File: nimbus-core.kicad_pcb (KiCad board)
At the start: 4 copper layers, 61.9 x 61.9 mm, 71 parts, among them J1 QTE-020-03-L-D-A, J2 QSE-020-01-L-D-A, J3 532614006, J4 USB4105-GF-A-120, J5 532614006, J6 532614006, U1 STM32F405VGT7, U10 Yellow, U4 SN65HVD233-Q1, U8 SN65HVD1782-Q1, U9 USBLC6-2P6, Y1 25MHz

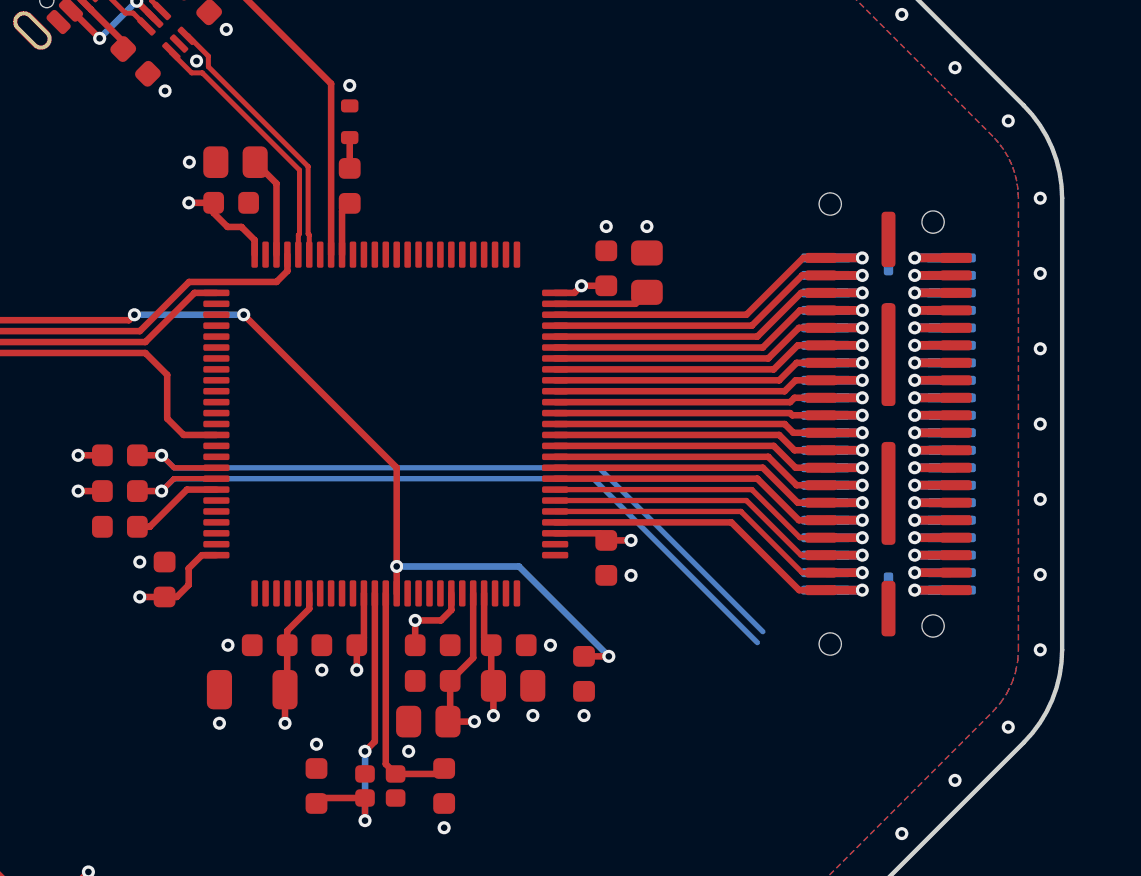
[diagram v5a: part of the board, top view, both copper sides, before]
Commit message: Moved passthrough connector to allow for connections on far the far side
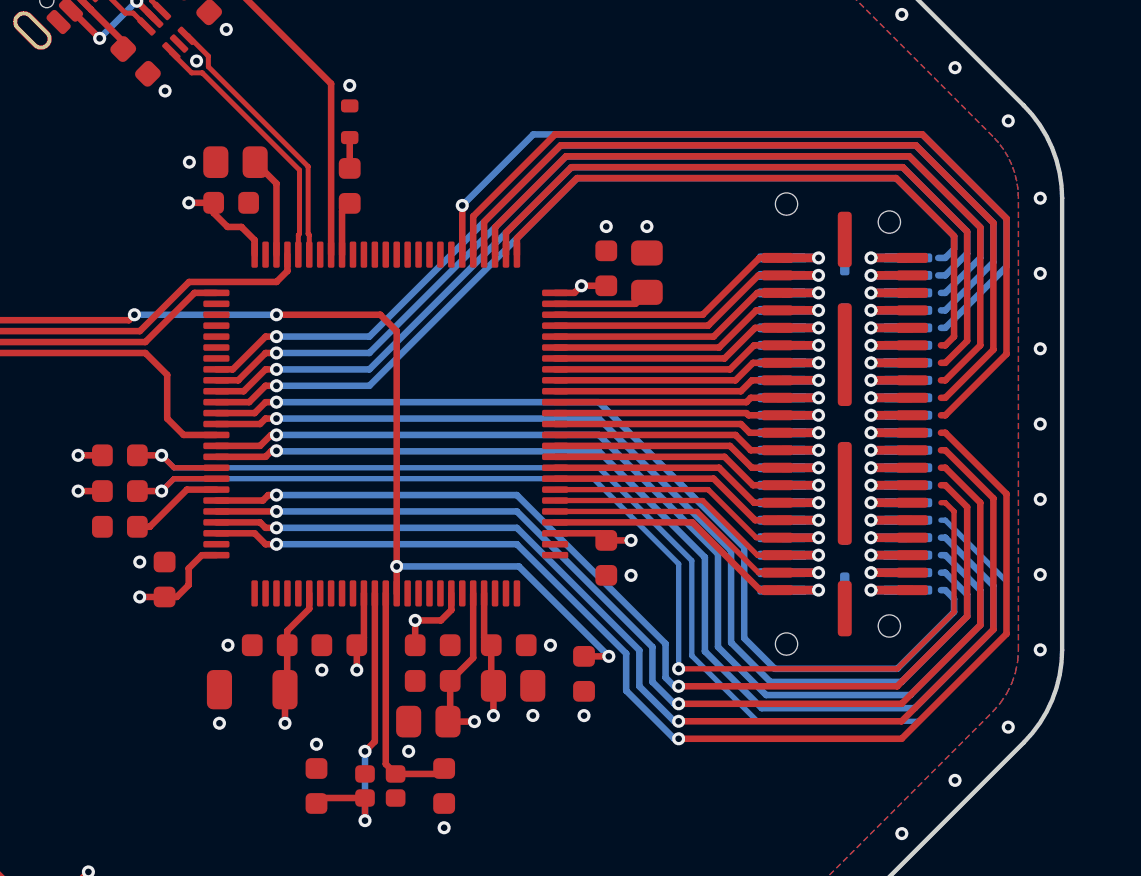
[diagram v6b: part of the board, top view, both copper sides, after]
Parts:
- moved J1 2.00 mm to (169.5, 105.0)
- moved J2 2.00 mm to (169.5, 105.0)
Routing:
- net unconnected-(U1F-PE1-Pad98): track 0.00 -> 53.6 mm, vias 0 -> 2
- net unconnected-(U1F-PE0-Pad97): track 0.00 -> 51.3 mm, vias 0 -> 2
- net unconnected-(U1C-PB5-Pad91): track 0.00 -> 49.9 mm, vias 0 -> 1
- net unconnected-(U1C-PB9-Pad96): track 0.00 -> 49.1 mm, vias 0 -> 2
- net unconnected-(U1C-PB4-Pad90): track 0.00 -> 48.0 mm, vias 0 -> 1
- net /PWR_ALERT: track 0.00 -> 46.9 mm, vias 0 -> 2
- net unconnected-(U1E-PD2-Pad83): track 0.00 -> 46.4 mm, vias 0 -> 1
- net unconnected-(U1E-PD7-Pad88): track 0.00 -> 45.8 mm, vias 0 -> 1
- net unconnected-(U1E-PD3-Pad84): track 0.00 -> 44.4 mm, vias 0 -> 1
- net /FIRE_PYRO1: track 0.00 -> 43.9 mm, vias 0 -> 1
- net unconnected-(U1E-PD4-Pad85): track 0.00 -> 42.6 mm, vias 0 -> 1
- net /FIRE_PYRO2: track 0.00 -> 40.6 mm, vias 0 -> 1
- net unconnected-(U1E-PD8-Pad55): track 0.00 -> 39.7 mm
- net unconnected-(U1C-PB15-Pad54): track 0.00 -> 36.8 mm
- net unconnected-(U1E-PD9-Pad56): track 0.00 -> 36.5 mm, vias 0 -> 1
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
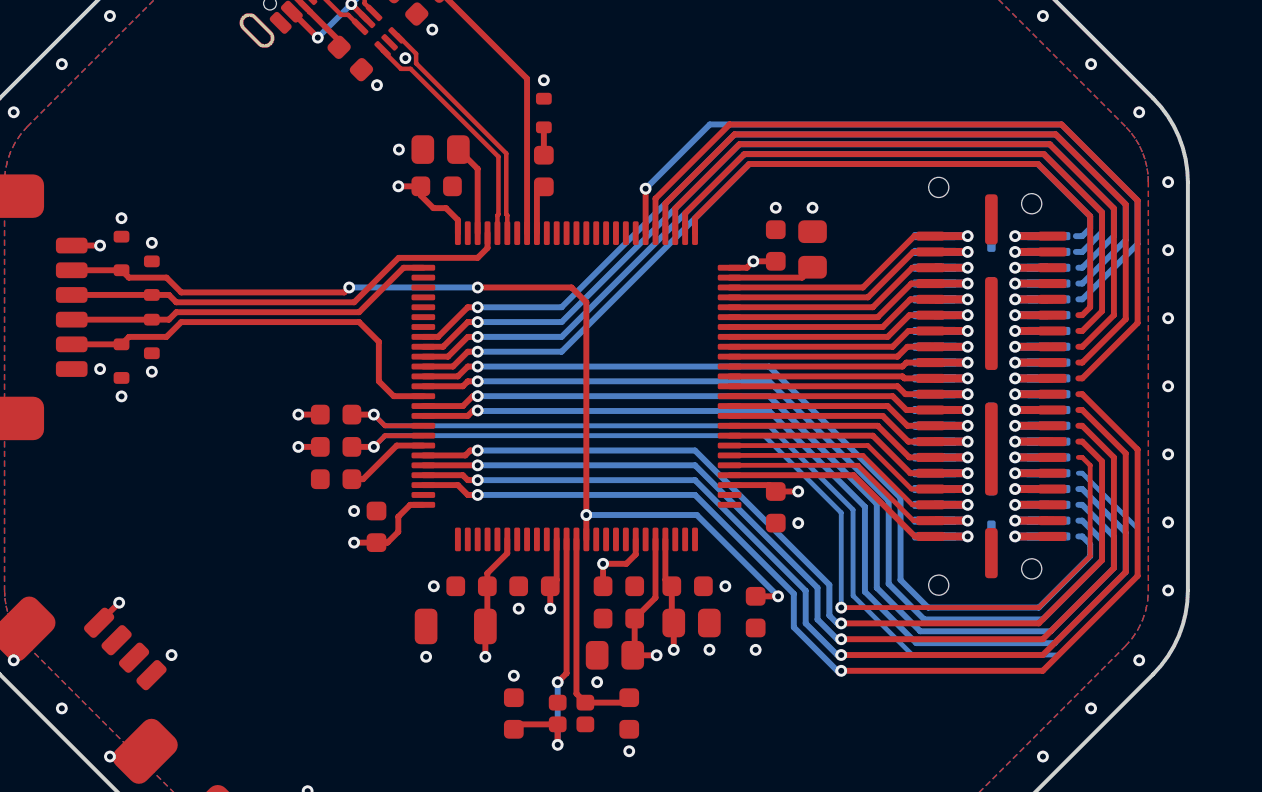
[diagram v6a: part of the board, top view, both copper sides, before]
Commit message: Rename all passthrough pins to their corresponding MCU pin name, fix typo on SPI pins
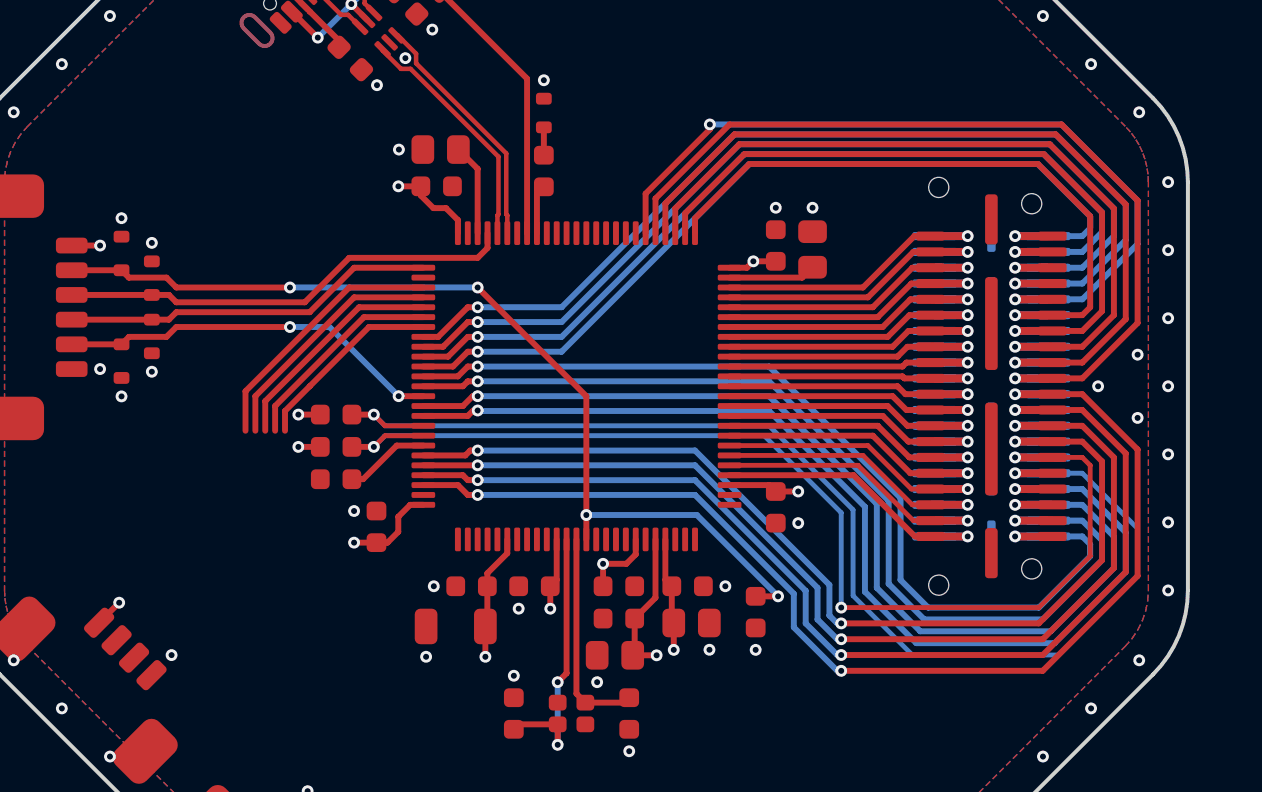
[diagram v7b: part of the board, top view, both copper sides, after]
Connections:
- net /ACCEL_IRQ renamed /PE9
- net /GNSS_RESET renamed /PA1
- net /GNSS_SAFEBOOT renamed /PA0
- net /GNSS_TIMEPULSE renamed /PA2
- net /IMU_IRQ renamed /PE7
- net /PASSTHROUGH_P16 renamed /PE10
- net /PASSTHROUGH_P2 renamed /PB11
- net /PASSTHROUGH_P24 renamed /PB2
- net /PASSTHROUGH_P26 renamed /PB1
- net /PASSTHROUGH_P28 renamed /PB0
- net /PASSTHROUGH_P30 renamed /PC5
- net /PASSTHROUGH_P34 renamed /SPI1_MOSI
- net /PASSTHROUGH_P36 renamed /SPI1_MISO
- net /PASSTHROUGH_P38 renamed /SPI1_SCK
- net /PASSTHROUGH_P4 renamed /PB10
- J1 pad 1: /PASSTHROUGH_P1 -> /PD5
- J1 pad 10: /PASSTHROUGH_P10 -> /PE13
- J1 pad 11: /PASSTHROUGH_P11 -> /PB12
- J1 pad 12: /PASSTHROUGH_P12 -> /PE12
- J1 pad 13: /PASSTHROUGH_P13 -> /PB13
- J1 pad 14: /PASSTHROUGH_P14 -> /PE11
- J1 pad 15: /PASSTHROUGH_P15 -> /PB14
- J1 pad 17: /PASSTHROUGH_P17 -> /PB15
- J1 pad 19: /PASSTHROUGH_P19 -> /PD8
- J1 pad 20: /PASSTHROUGH_P20 -> /PE8
- J1 pad 21: /PASSTHROUGH_P21 -> /PE1
- J1 pad 23: /PASSTHROUGH_P23 -> /PE0
- J1 pad 25: /PASSTHROUGH_P25 -> /PB9
- J1 pad 27: /PASSTHROUGH_P27 -> /PB8
- J1 pad 29: /PASSTHROUGH_P29 -> /I2C1_SDA
- J1 pad 3: /PASSTHROUGH_P3 -> /PD4
- J1 pad 31: /PASSTHROUGH_P31 -> /I2C1_SCL
- J1 pad 32: /PASSTHROUGH_P32 -> /PC4
- J1 pad 33: /PASSTHROUGH_P33 -> /PB5
- J1 pad 35: /PASSTHROUGH_P35 -> /PB4
- J1 pad 37: /PASSTHROUGH_P37 -> /PD7
- J1 pad 39: /PASSTHROUGH_P39 -> /PD6
- J1 pad 40: /PASSTHROUGH_P40 -> /PA4
- J1 pad 5: /PASSTHROUGH_P5 -> /PD3
- J1 pad 6: /PASSTHROUGH_P6 -> /PE15
- J1 pad 7: /PASSTHROUGH_P7 -> /PD2
- J1 pad 8: /PASSTHROUGH_P8 -> /PE14
- J1 pad 9: /PASSTHROUGH_P9 -> /PD9
- J2 pad 1: /PASSTHROUGH_P1 -> /PD5
- J2 pad 10: /PASSTHROUGH_P10 -> /PE13
- J2 pad 11: /PASSTHROUGH_P11 -> /PB12
- J2 pad 12: /PASSTHROUGH_P12 -> /PE12
- J2 pad 13: /PASSTHROUGH_P13 -> /PB13
- J2 pad 14: /PASSTHROUGH_P14 -> /PE11
- J2 pad 15: /PASSTHROUGH_P15 -> /PB14
- J2 pad 17: /PASSTHROUGH_P17 -> /PB15
- J2 pad 19: /PASSTHROUGH_P19 -> /PD8
- J2 pad 20: /PASSTHROUGH_P20 -> /PE8
- J2 pad 21: /PASSTHROUGH_P21 -> /PE1
- J2 pad 23: /PASSTHROUGH_P23 -> /PE0
- J2 pad 25: /PASSTHROUGH_P25 -> /PB9
- J2 pad 27: /PASSTHROUGH_P27 -> /PB8
- J2 pad 29: /PASSTHROUGH_P29 -> /I2C1_SDA
- J2 pad 3: /PASSTHROUGH_P3 -> /PD4
- J2 pad 31: /PASSTHROUGH_P31 -> /I2C1_SCL
- J2 pad 32: /PASSTHROUGH_P32 -> /PC4
- J2 pad 33: /PASSTHROUGH_P33 -> /PB5
- J2 pad 35: /PASSTHROUGH_P35 -> /PB4
- J2 pad 37: /PASSTHROUGH_P37 -> /PD7
- J2 pad 39: /PASSTHROUGH_P39 -> /PD6
- J2 pad 40: /PASSTHROUGH_P40 -> /PC4
- J2 pad 5: /PASSTHROUGH_P5 -> /PD3
- J2 pad 6: /PASSTHROUGH_P6 -> /PE15
- J2 pad 7: /PASSTHROUGH_P7 -> /PD2
- J2 pad 8: /PASSTHROUGH_P8 -> /PE14
- J2 pad 9: /PASSTHROUGH_P9 -> /PD9
- U1 pad 1: unconnected-(U1F-PE2-Pad1) -> /PE2
- U1 pad 15: unconnected-(U1D-PC0-Pad15) -> /PC0
- U1 pad 16: unconnected-(U1D-PC1-Pad16) -> /PC1
- U1 pad 17: unconnected-(U1D-PC2-Pad17) -> /PC2
- U1 pad 18: unconnected-(U1D-PC3-Pad18) -> /PC3
- U1 pad 2: unconnected-(U1F-PE3-Pad2) -> /PE3
- U1 pad 26: /~{GNSS_SS} -> /PA3
- U1 pad 29: /PASSTHROUGH_P40 -> /PA4
- U1 pad 3: unconnected-(U1F-PE4-Pad3) -> /PE4
- U1 pad 33: /PASSTHROUGH_P32 -> /PC4
- U1 pad 39: /PASSTHROUGH_P20 -> /PE8
- U1 pad 4: unconnected-(U1F-PE5-Pad4) -> /PE5
- U1 pad 42: /PASSTHROUGH_P14 -> /PE11
- U1 pad 43: /PASSTHROUGH_P12 -> /PE12
- U1 pad 44: /PASSTHROUGH_P10 -> /PE13
- U1 pad 45: /PASSTHROUGH_P8 -> /PE14
- U1 pad 46: /PASSTHROUGH_P6 -> /PE15
- U1 pad 5: unconnected-(U1F-PE6-Pad5) -> /PE6
- U1 pad 51: /RADIO_RESET -> /PB12
- U1 pad 52: /RADIO_ANT_EN -> /PB13
- U1 pad 53: unconnected-(U1C-PB14-Pad53) -> /PB14
- U1 pad 54: unconnected-(U1C-PB15-Pad54) -> /PB15
- U1 pad 55: unconnected-(U1E-PD8-Pad55) -> /PD8
- U1 pad 56: unconnected-(U1E-PD9-Pad56) -> /PD9
- U1 pad 57: unconnected-(U1E-PD10-Pad57) -> /PD10
- U1 pad 58: unconnected-(U1E-PD11-Pad58) -> /PD11
- U1 pad 59: unconnected-(U1E-PD12-Pad59) -> /PD12
- U1 pad 60: unconnected-(U1E-PD13-Pad60) -> /PD13
- U1 pad 61: unconnected-(U1E-PD14-Pad61) -> /PD14
- U1 pad 62: unconnected-(U1E-PD15-Pad62) -> /PD15
- U1 pad 63: unconnected-(U1D-PC6-Pad63) -> /PC6
- U1 pad 64: unconnected-(U1D-PC7-Pad64) -> /PC7
- U1 pad 65: unconnected-(U1D-PC8-Pad65) -> /PC8
- U1 pad 66: unconnected-(U1D-PC9-Pad66) -> /PC9
- U1 pad 69: unconnected-(U1B-PA10-Pad69) -> /PA10
- U1 pad 7: unconnected-(U1D-PC13-Pad7) -> /PC13
- U1 pad 8: unconnected-(U1D-PC14-Pad8) -> /PC14
- U1 pad 83: unconnected-(U1E-PD2-Pad83) -> /PD2
- U1 pad 84: unconnected-(U1E-PD3-Pad84) -> /PD3
- U1 pad 85: unconnected-(U1E-PD4-Pad85) -> /PD4
- U1 pad 86: /FIRE_PYRO2 -> /PD5
- U1 pad 87: /FIRE_PYRO1 -> /PD6
- U1 pad 88: unconnected-(U1E-PD7-Pad88) -> /PD7
- U1 pad 9: unconnected-(U1D-PC15-Pad9) -> /PC15
- U1 pad 90: unconnected-(U1C-PB4-Pad90) -> /PB4
- U1 pad 91: unconnected-(U1C-PB5-Pad91) -> /PB5
- U1 pad 95: /PWR_ALERT -> /PB8
- U1 pad 96: unconnected-(U1C-PB9-Pad96) -> /PB9
- U1 pad 97: unconnected-(U1F-PE0-Pad97) -> /PE0
- U1 pad 98: unconnected-(U1F-PE1-Pad98) -> /PE1
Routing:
- net /PE1: track 0.00 -> 58.5 mm, vias 0 -> 3
- net /PE0: track 0.00 -> 56.2 mm, vias 0 -> 3
- net /PB5: track 0.00 -> 54.9 mm, vias 0 -> 2
- net /PB9: track 0.00 -> 54.0 mm, vias 0 -> 3
- net unconnected-(U1F-PE1-Pad98): track 53.6 -> 0.00 mm, vias 2 -> 0
- net /PB4: track 0.00 -> 53.0 mm, vias 0 -> 2
- net /PB8: track 0.00 -> 51.8 mm, vias 0 -> 3
- net /PD2: track 0.00 -> 51.5 mm, vias 0 -> 2
- net unconnected-(U1F-PE0-Pad97): track 51.3 -> 0.00 mm, vias 2 -> 0
- net /PD7: track 0.00 -> 50.8 mm, vias 0 -> 2
- net unconnected-(U1C-PB5-Pad91): track 49.9 -> 0.00 mm, vias 1 -> 0
- net /PD3: track 0.00 -> 49.5 mm, vias 0 -> 2
- net unconnected-(U1C-PB9-Pad96): track 49.1 -> 0.00 mm, vias 2 -> 0
- net /PD6: track 0.00 -> 49.0 mm, vias 0 -> 2
- net unconnected-(U1C-PB4-Pad90): track 48.0 -> 0.00 mm, vias 1 -> 0
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
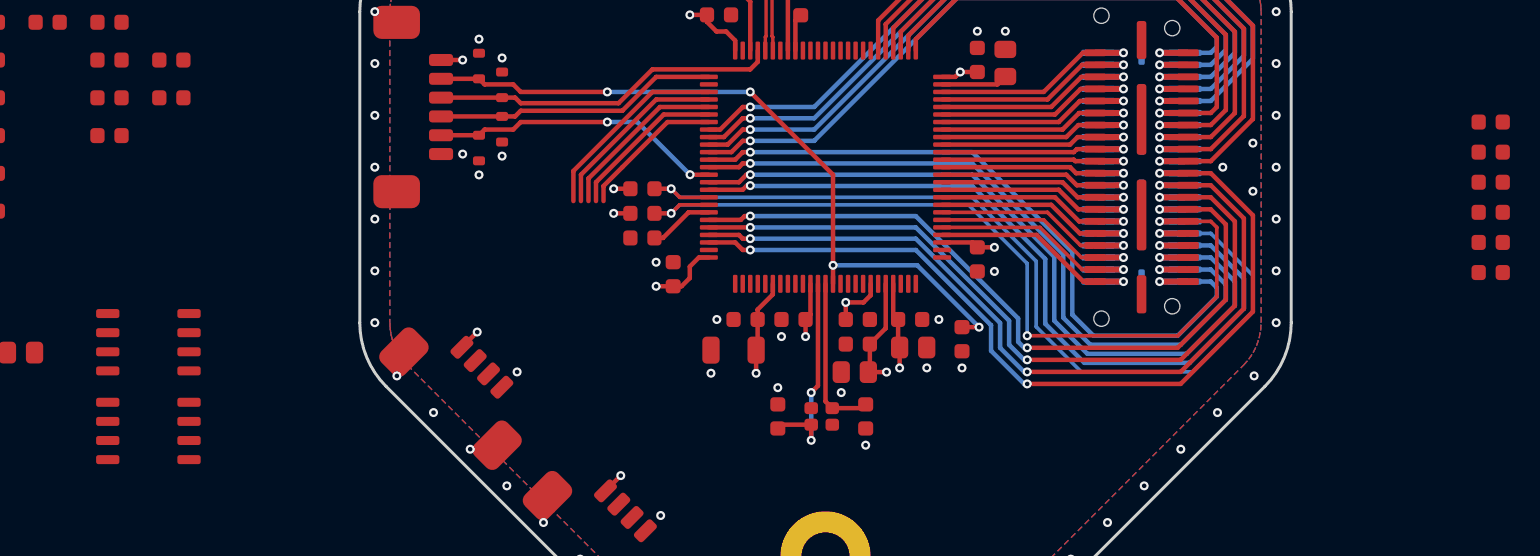
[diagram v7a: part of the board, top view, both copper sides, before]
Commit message: Updated kicad-library
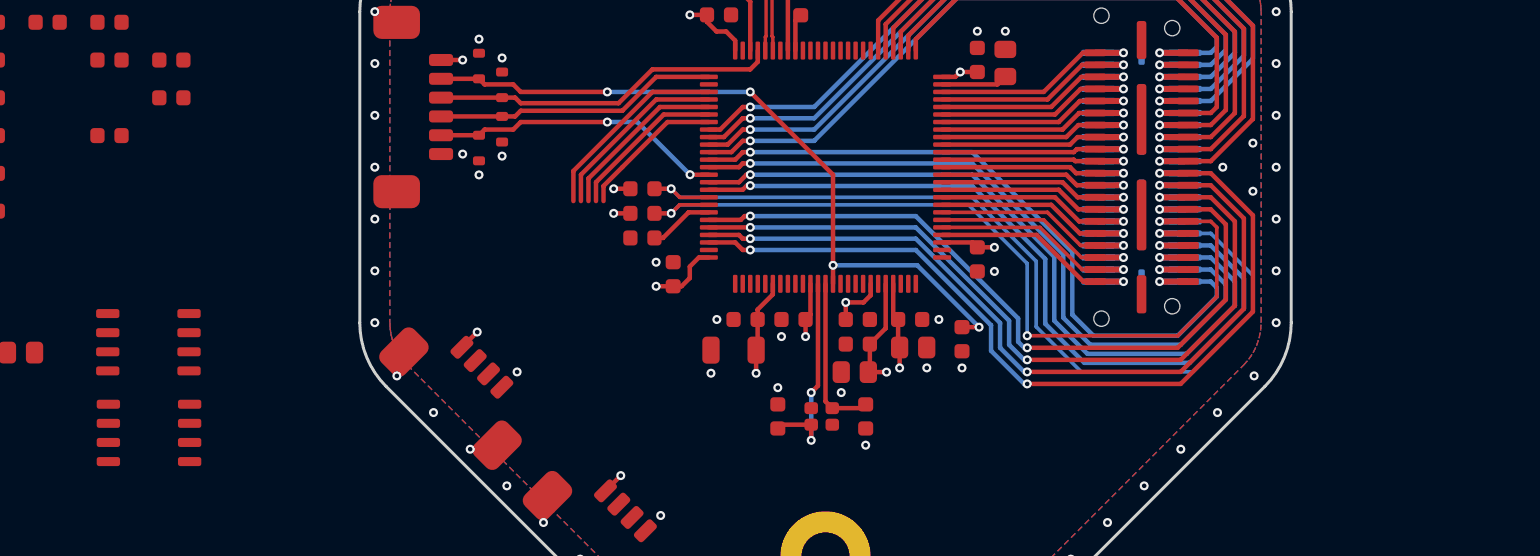
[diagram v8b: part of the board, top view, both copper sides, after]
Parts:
- removed the R10 at (192.7, 102.0)
- removed the R17 at (100.9, 100.4)
- removed the R2 at (192.7, 112.0)
- removed the R6 at (192.7, 110.0)
- removed the R7 at (192.7, 108.0)
- removed the R8 at (192.7, 106.0)
- removed the R9 at (192.7, 104.0)
- moved U2 0.14 mm to (103.5, 122.7)
- renumbered R16 to R10, R18 to R11, R19 to R12, R20 to R13, R21 to R14, R22 to R15, R23 to R16, R24 to R17, R25 to R18, R26 to R19, R3 to R2, R27 to R20, R4 to R3, R5 to R4, R11 to R5, R12 to R6, R13 to R7, R14 to R8, R15 to R9, U4 to U2, U8 to U3, U9 to U4, U10 to U5
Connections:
- J2 pad 40: /PC4 -> /PA4
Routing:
- net /PA4: track 0.00 -> 15.0 mm, vias 0 -> 1
- net (no net): track 15.0 -> 0.00 mm
- net /PC4: vias 2 -> 1
